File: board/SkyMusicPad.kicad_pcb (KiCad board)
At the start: 2 copper layers, 119.4 x 61 mm, 32 parts, among them SW1 RotaryEncoder_Switch

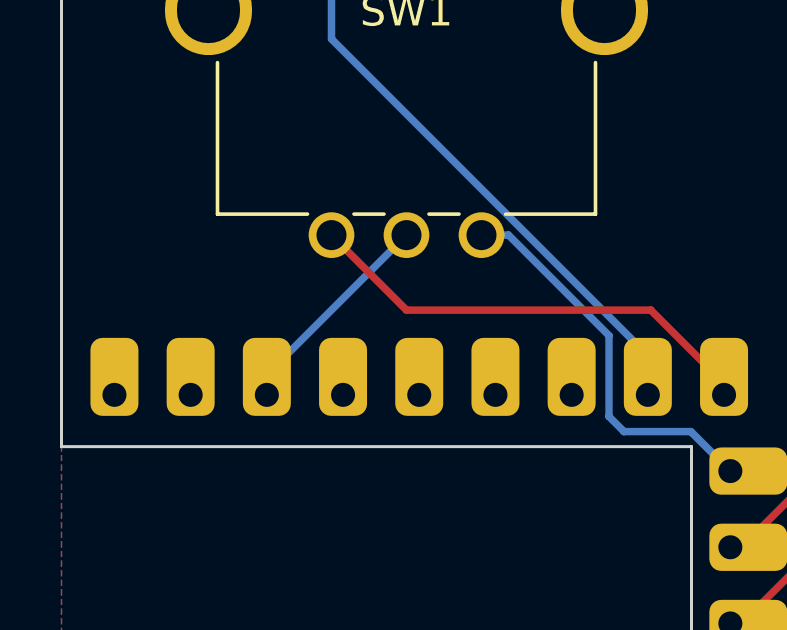
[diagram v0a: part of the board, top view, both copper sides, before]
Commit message: Adjusted rotary encoder to have common point GND
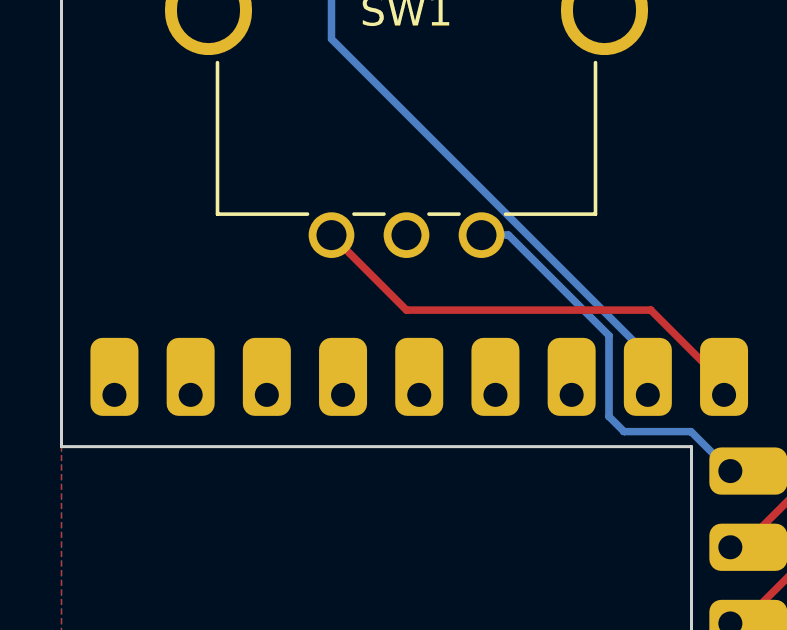
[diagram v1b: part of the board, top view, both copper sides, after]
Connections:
- SW1 pad C: +3.3V -> GND
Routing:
- net +3.3V: track 7.25 -> 0.00 mm
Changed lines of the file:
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@@
       (net 13 "Net-(RZ1-GP13)") (pinfunction "B") (pintype "passive"))
     (pad "C" thru_hole circle (at 0 2.5) (size 1.524 1.524) (drill 1) (layers "*.Cu" "*.Mask")
-      (net 9 "+3.3V") (pinfunction "C") (pintype "passive"))
+      (net 11 "GND") (pinfunction "C") (pintype "passive"))
     (pad "S1" thru_hole circle (at 14.5 0) (size 1.524 1.524) (drill 1) (layers "*.Cu" "*.Mask")
       (net 14 "Net-(RZ1-GP15)") (pinfunction "S1") (pintype "passive"))
@@
   (via (at 109 69.5) (size 0.8) (drill 0.4) (layers "F.Cu" "B.Cu") (net 8))
   (via (at 72.5 69.5) (size 0.8) (drill 0.4) (layers "F.Cu" "B.Cu") (net 8))
-  (segment (start 31.5 47.95) (end 26.845 52.605) (width 0.25) (layer "B.Cu") (net 9))
-  (segment (start 26.845 52.605) (end 26.845 53.275) (width 0.25) (layer "B.Cu") (net 9))
   (segment (start 29 47.95) (end 31.5 50.45) (width 0.25) (layer "F.Cu") (net 12))
   (segment (start 39.645376 50.45) (end 42.085 52.889624) (width 0.25) (layer "F.Cu") (net 12))

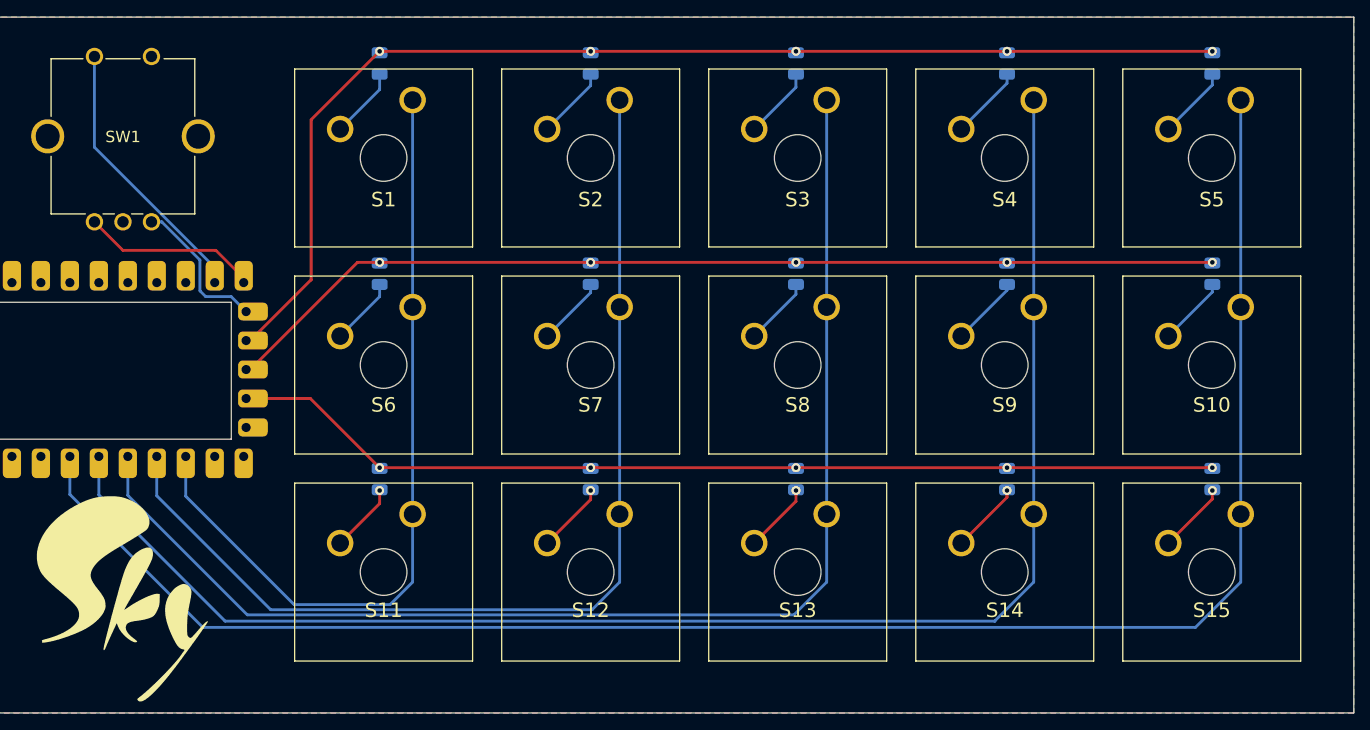
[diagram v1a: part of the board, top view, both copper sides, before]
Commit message: Fixed the use of the incorrect footprint for MX
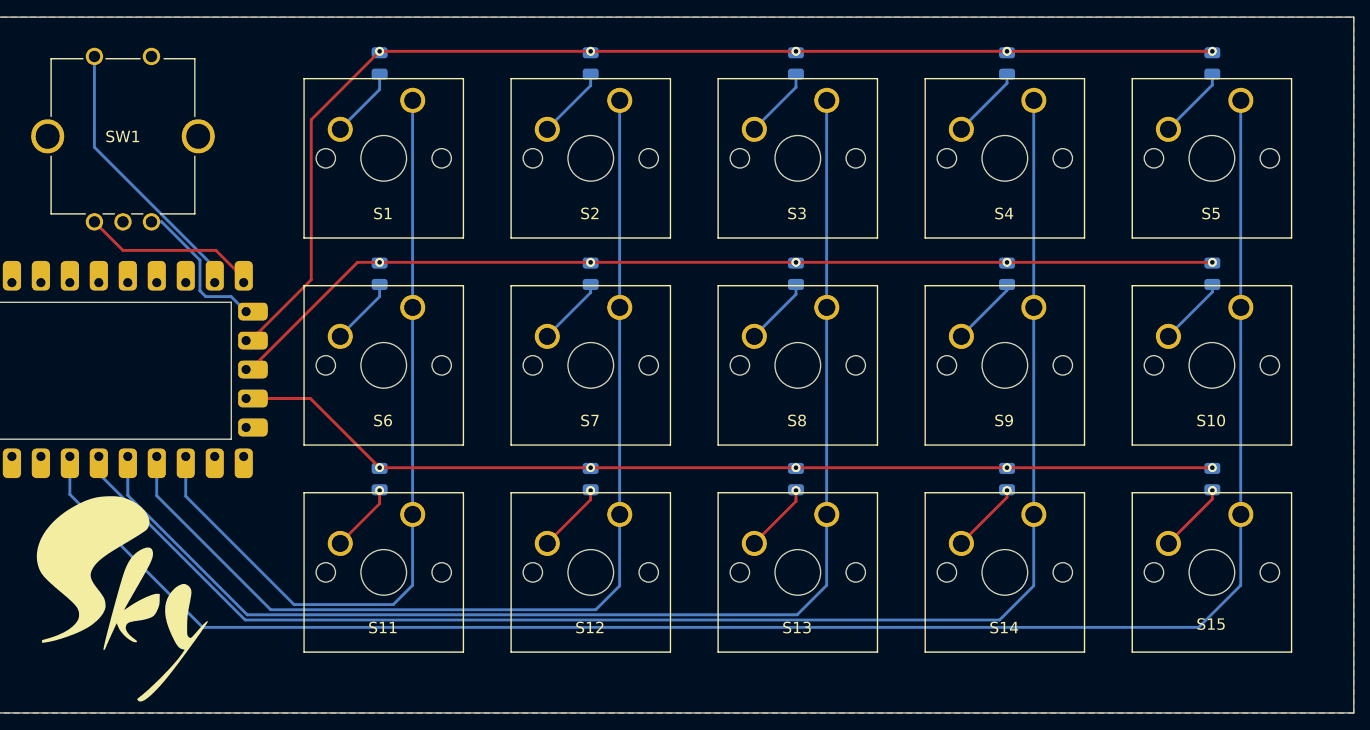
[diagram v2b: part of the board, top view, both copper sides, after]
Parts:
- S1, S10, S11, S12, S13, S14, S15, S2, S3, S4, S5, S6, S7, S8, S9: footprint MX1A-C1NN:MX1AC1NN -> Button_Switch_Keyboard:SW_Cherry_MX_1.00u_PCB
- moved S1 6.84 mm to (56.9, 37.3)
- moved S11 6.84 mm to (56.9, 73.6)
- moved S12 6.84 mm to (75.0, 73.6)
- moved S13 6.84 mm to (93.2, 73.6)
- moved S14 6.84 mm to (111.3, 73.6)
- moved S15 6.84 mm to (129.5, 73.6)
- moved S2 6.84 mm to (75.0, 37.3)
- moved S3 6.84 mm to (93.2, 37.3)
- moved S4 6.84 mm to (111.3, 37.3)
- moved S5 6.84 mm to (129.5, 37.3)
- moved S10 6.84 mm to (129.5, 55.5)
- moved S6 6.84 mm to (56.9, 55.5)
- moved S7 6.84 mm to (75.0, 55.5)
- moved S8 6.84 mm to (93.2, 55.5)
- moved S9 6.84 mm to (111.3, 55.5)
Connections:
- S1 pad 1: Net-(D1-A) -> Col0
- S1 pad 2: Col0 -> Net-(D1-A)
- S11 pad 1: Net-(D3-A) -> Col0
- S11 pad 2: Col0 -> Net-(D3-A)
- S12 pad 1: Net-(D6-A) -> Col1
- S12 pad 2: Col1 -> Net-(D6-A)
- S13 pad 1: Net-(D9-A) -> Col2
- S13 pad 2: Col2 -> Net-(D9-A)
- S14 pad 1: Net-(D12-A) -> Col3
- S14 pad 2: Col3 -> Net-(D12-A)
- S2 pad 1: Net-(D4-A) -> Col1
- S2 pad 2: Col1 -> Net-(D4-A)
- S3 pad 1: Net-(D7-A) -> Col2
- S3 pad 2: Col2 -> Net-(D7-A)
- S4 pad 1: Net-(D10-A) -> Col3
- S4 pad 2: Col3 -> Net-(D10-A)
- S6 pad 1: Net-(D2-A) -> Col0
- S6 pad 2: Col0 -> Net-(D2-A)
- S7 pad 1: Net-(D5-A) -> Col1
- S7 pad 2: Col1 -> Net-(D5-A)
- S8 pad 1: Net-(D8-A) -> Col2
- S8 pad 2: Col2 -> Net-(D8-A)
- S9 pad 1: Net-(D11-A) -> Col3
- S9 pad 2: Col3 -> Net-(D11-A)
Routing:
- net Col3: track 133.6 -> 132.6 mm

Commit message: a
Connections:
- S10 pad 1: Net-(D14-A) -> Col4
- S10 pad 2: Col4 -> Net-(D14-A)
- S15 pad 1: Net-(D15-A) -> Col4
- S15 pad 2: Col4 -> Net-(D15-A)
- S5 pad 1: Net-(D13-A) -> Col4
- S5 pad 2: Col4 -> Net-(D13-A)
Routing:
- net Col3: track 132.6 -> 134.1 mm
- net Net-(D9-A): track 6.13 -> 6.21 mm, vias 1 -> 0
- net Net-(D3-A): track 6.04 -> 6.13 mm, vias 1 -> 0
- net Net-(D6-A): track 6.19 -> 6.28 mm, vias 1 -> 0
- net Net-(D15-A): track 6.21 -> 6.30 mm, vias 1 -> 0
- net Net-(D12-A): track 6.27 -> 6.36 mm, vias 1 -> 0
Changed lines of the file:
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@@
     (pad "" np_thru_hole circle (at 2.54 5.08) (size 1.7 1.7) (drill 1.7) (layers "*.Cu" "*.Mask"))
     (pad "1" thru_hole circle (at 0 0) (size 2.2 2.2) (drill 1.5) (layers "*.Cu" "*.Mask")
-      (net 29 "Net-(D15-A)") (pinfunction "1") (pintype "passive"))
+      (net 5 "Col4") (pinfunction "1") (pintype "passive"))
     (pad "2" thru_hole circle (at -6.35 2.54) (size 2.2 2.2) (drill 1.5) (layers "*.Cu" "*.Mask")
-      (net 5 "Col4") (pinfunction "2") (pintype "passive"))
+      (net 29 "Net-(D15-A)") (pinfunction "2") (pintype "passive"))
     (model "${KICAD6_3DMODEL_DIR}/Button_Switch_Keyboard.3dshapes/SW_Cherry_MX_1.00u_PCB.wrl"
       (offset (xyz 0 0 0))
@@
     (pad "" np_thru_hole circle (at 2.54 5.08) (size 1.7 1.7) (drill 1.7) (layers "*.Cu" "*.Mask"))
     (pad "1" thru_hole circle (at 0 0) (size 2.2 2.2) (drill 1.5) (layers "*.Cu" "*.Mask")
-      (net 27 "Net-(D13-A)") (pinfunction "1") (pintype "passive"))
+      (net 5 "Col4") (pinfunction "1") (pintype "passive"))
     (pad "2" thru_hole circle (at -6.35 2.54) (size 2.2 2.2) (drill 1.5) (layers "*.Cu" "*.Mask")
-      (net 5 "Col4") (pinfunction "2") (pintype "passive"))
+      (net 27 "Net-(D13-A)") (pinfunction "2") (pintype "passive"))
     (model "${KICAD6_3DMODEL_DIR}/Button_Switch_Keyboard.3dshapes/SW_Cherry_MX_1.00u_PCB.wrl"
       (offset (xyz 0 0 0))
@@
     (pad "" np_thru_hole circle (at 2.54 5.08) (size 1.7 1.7) (drill 1.7) (layers "*.Cu" "*.Mask"))
     (pad "1" thru_hole circle (at 0 0) (size 2.2 2.2) (drill 1.5) (layers "*.Cu" "*.Mask")
-      (net 28 "Net-(D14-A)") (pinfunction "1") (pintype "passive"))
+      (net 5 "Col4") (pinfunction "1") (pintype "passive"))
     (pad "2" thru_hole circle (at -6.35 2.54) (size 2.2 2.2) (drill 1.5) (layers "*.Cu" "*.Mask")
-      (net 5 "Col4") (pinfunction "2") (pintype "passive"))
+      (net 28 "Net-(D14-A)") (pinfunction "2") (pintype "passive"))
     (model "${KICAD6_3DMODEL_DIR}/Button_Switch_Keyboard.3dshapes/SW_Cherry_MX_1.00u_PCB.wrl"
       (offset (xyz 0 0 0))
@@
   (gr_line (start 20 67) (end 41 67)
     (stroke (width 0.1) (type default)) (layer "Edge.Cuts"))
-  (segment (start 55.2 81.5) (end 46.5 81.5) (width 0.25) (layer "B.Cu") (net 1))
   (segment (start 56.89 37.27) (end 56.89 79.81) (width 0.25) (layer "B.Cu") (net 1))
-  (segment (start 37.005 72.005) (end 37.005 68.515) (width 0.25) (layer "B.Cu") (net 1))
-  (segment (start 56.89 79.81) (end 55.2 81.5) (width 0.25) (layer "B.Cu") (net 1))
-  (segment (start 46.5 81.5) (end 37.005 72.005) (width 0.25) (layer "B.Cu") (net 1))
-  (segment (start 72.95 81.95) (end 44.45 81.95) (width 0.25) (layer "B.Cu") (net 2))
+  (segment (start 47.005 82) (end 37.005 72) (width 0.25) (layer "B.Cu") (net 1))
+  (segment (start 56.89 79.81) (end 54.7 82) (width 0.25) (layer "B.Cu") (net 1))
+  (segment (start 37.005 72) (end 37.005 68.515) (width 0.25) (layer "B.Cu") (net 1))
+  (segment (start 37.005 72.005) (end 37.005 72) (width 0.25) (layer "B.Cu") (net 1))
+  (segment (start 54.7 82) (end 47.005 82) (width 0.25) (layer "B.Cu") (net 1))
+  (segment (start 44.95 82.45) (end 34.465 71.965) (width 0.25) (layer "B.Cu") (net 2))
   (segment (start 75.04 37.27) (end 75.04 79.86) (width 0.25) (layer "B.Cu") (net 2))
-  (segment (start 44.45 81.95) (end 34.465 71.965) (width 0.25) (layer "B.Cu") (net 2))
+  (segment (start 75.04 79.86) (end 72.45 82.45) (width 0.25) (layer "B.Cu") (net 2))
   (segment (start 34.465 71.965) (end 34.465 68.515) (width 0.25) (layer "B.Cu") (net 2))
-  (segment (start 75.04 79.86) (end 72.95 81.95) (width 0.25) (layer "B.Cu") (net 2))
+  (segment (start 72.45 82.45) (end 44.95 82.45) (width 0.25) (layer "B.Cu") (net 2))
+  (segment (start 93.19 79.81) (end 90.1 82.9) (width 0.25) (layer "B.Cu") (net 3))
+  (segment (start 90.1 82.9) (end 42.9 82.9) (width 0.25) (layer "B.Cu") (net 3))
   (segment (start 31.925 71.925) (end 31.925 68.515) (width 0.25) (layer "B.Cu") (net 3))
-  (segment (start 90.6 82.4) (end 42.4 82.4) (width 0.25) (layer "B.Cu") (net 3))
-  (segment (start 42.4 82.4) (end 31.925 71.925) (width 0.25) (layer "B.Cu") (net 3))
   (segment (start 93.19 37.27) (end 93.19 79.81) (width 0.25) (layer "B.Cu") (net 3))
-  (segment (start 93.19 79.81) (end 90.6 82.4) (width 0.25) (layer "B.Cu") (net 3))
-  (segment (start 42.213604 82.85) (end 108.35 82.85) (width 0.25) (layer "B.Cu") (net 4))
-  (segment (start 29.385 70.021396) (end 42.213604 82.85) (width 0.25) (layer "B.Cu") (net 4))
-  (segment (start 29.385 68.515) (end 29.385 70.021396) (width 0.25) (layer "B.Cu") (net 4))
+  (segment (start 42.9 82.9) (end 31.925 71.925) (width 0.25) (layer "B.Cu") (net 3))
   (segment (start 111.34 79.86) (end 111.34 37.27) (width 0.25) (layer "B.Cu") (net 4))
-  (segment (start 108.35 82.85) (end 111.34 79.86) (width 0.25) (layer "B.Cu") (net 4))
+  (segment (start 111.34 79.86) (end 107.85 83.35) (width 0.25) (layer "B.Cu") (net 4))
+  (segment (start 29.385 68.515) (end 29.385 71.75) (width 0.25) (layer "B.Cu") (net 4))
+  (segment (start 107.85 83.35) (end 40.985 83.35) (width 0.25) (layer "B.Cu") (net 4))
+  (segment (start 40.985 83.35) (end 29.385 71.75) (width 0.25) (layer "B.Cu") (net 4))
+  (segment (start 29.385 71.75) (end 29.385 71.845) (width 0.25) (layer "B.Cu") (net 4))
   (segment (start 26.845 71.845) (end 26.845 68.515) (width 0.25) (layer "B.Cu") (net 5))
   (segment (start 129.49 73.57) (end 129.49 37.27) (width 0.25) (layer "B.Cu") (net 5))
-  (segment (start 129.49 79.81) (end 125.8 83.5) (width 0.25) (layer "B.Cu") (net 5))
+  (segment (start 129.49 79.81) (end 125.5 83.8) (width 0.25) (layer "B.Cu") (net 5))
+  (segment (start 125.5 83.8) (end 38.8 83.8) (width 0.25) (layer "B.Cu") (net 5))
   (segment (start 129.49 73.57) (end 129.49 79.81) (width 0.25) (layer "B.Cu") (net 5))
-  (segment (start 38.5 83.5) (end 26.845 71.845) (width 0.25) (layer "B.Cu") (net 5))
-  (segment (start 125.8 83.5) (end 38.5 83.5) (width 0.25) (layer "B.Cu") (net 5))
+  (segment (start 38.8 83.8) (end 26.845 71.845) (width 0.25) (layer "B.Cu") (net 5))
   (segment (start 129.49 73.57) (end 129.5 73.58) (width 0.25) (layer "B.Cu") (net 5))
   (segment (start 48 39) (end 54 33) (width 0.25) (layer "F.Cu") (net 6))
@@
   (segment (start 54 53.4375) (end 54 54.5) (width 0.25) (layer "B.Cu") (net 16))
   (segment (start 54 54.5) (end 50.54 57.96) (width 0.25) (layer "B.Cu") (net 16))
-  (segment (start 54 71.5) (end 54 72.65) (width 0.25) (layer "F.Cu") (net 17))
-  (segment (start 54 72.65) (end 50.54 76.11) (width 0.25) (layer "F.Cu") (net 17))
-  (via (at 54 71.5) (size 0.8) (drill 0.4) (layers "F.Cu" "B.Cu") (net 17))
+  (segment (start 50.55 76.14) (end 54 72.69) (width 0.25) (layer "B.Cu") (net 17))
+  (segment (start 54 72.69) (end 54 71.4375) (width 0.25) (layer "B.Cu") (net 17))
   (segment (start 72.5 36) (end 68.69 39.81) (width 0.25) (layer "B.Cu") (net 18))
   (segment (start 72.5 35) (end 72.5 36) (width 0.25) (layer "B.Cu") (net 18))
   (segment (start 72.5 54.15) (end 68.69 57.96) (width 0.25) (layer "B.Cu") (net 19))
   (segment (start 72.5 53.4375) (end 72.5 54.15) (width 0.25) (layer "B.Cu") (net 19))
-  (segment (start 72.5 72.3) (end 68.69 76.11) (width 0.25) (layer "F.Cu") (net 20))
-  (segment (start 72.5 71.5) (end 72.5 72.3) (width 0.25) (layer "F.Cu") (net 20))
-  (via (at 72.5 71.5) (size 0.8) (drill 0.4) (layers "F.Cu" "B.Cu") (net 20))
+  (segment (start 68.7 76.14) (end 72.5 72.34) (width 0.25) (layer "B.Cu") (net 20))
+  (segment (start 72.5 72.34) (end 72.5 71.4375) (width 0.25) (layer "B.Cu") (net 20))
   (segment (start 90.5 35) (end 90.5 36.15) (width 0.25) (layer "B.Cu") (net 21))
   (segment (start 90.5 36.15) (end 86.84 39.81) (width 0.25) (layer "B.Cu") (net 21))
   (segment (start 90.5 53.4375) (end 90.5 54.3) (width 0.25) (layer "B.Cu") (net 22))
   (segment (start 90.5 54.3) (end 86.84 57.96) (width 0.25) (layer "B.Cu") (net 22))
-  (segment (start 90.5 72.45) (end 86.84 76.11) (width 0.25) (layer "F.Cu") (net 23))
-  (segment (start 90.5 71.5) (end 90.5 72.45) (width 0.25) (layer "F.Cu") (net 23))
-  (via (at 90.5 71.5) (size 0.8) (drill 0.4) (layers "F.Cu" "B.Cu") (net 23))
+  (segment (start 86.85 76.14) (end 90.5 72.49) (width 0.25) (layer "B.Cu") (net 23))
+  (segment (start 90.5 72.49) (end 90.5 71.4375) (width 0.25) (layer "B.Cu") (net 23))
   (segment (start 109 35) (end 109 35.8) (width 0.25) (layer "B.Cu") (net 24))
   (segment (start 109 35.8) (end 104.99 39.81) (width 0.25) (layer "B.Cu") (net 24))
   (segment (start 109 53.4375) (end 109 53.95) (width 0.25) (layer "B.Cu") (net 25))
   (segment (start 109 53.95) (end 104.99 57.96) (width 0.25) (layer "B.Cu") (net 25))
-  (segment (start 109 71.5) (end 109 72.1) (width 0.25) (layer "F.Cu") (net 26))
-  (segment (start 109 72.1) (end 104.99 76.11) (width 0.25) (layer "F.Cu") (net 26))
-  (via (at 109 71.5) (size 0.8) (drill 0.4) (layers "F.Cu" "B.Cu") (net 26))
+  (segment (start 109 72.14) (end 109 71.4375) (width 0.25) (layer "B.Cu") (net 26))
+  (segment (start 105 76.14) (end 109 72.14) (width 0.25) (layer "B.Cu") (net 26))
   (segment (start 127 35) (end 127 35.95) (width 0.25) (layer "B.Cu") (net 27))
   (segment (start 127 35.95) (end 123.14 39.81) (width 0.25) (layer "B.Cu") (net 27))
   (segment (start 127 53.4375) (end 127 54.1) (width 0.25) (layer "B.Cu") (net 28))
   (segment (start 127 54.1) (end 123.14 57.96) (width 0.25) (layer "B.Cu") (net 28))
-  (segment (start 127 71.5) (end 127 72.25) (width 0.25) (layer "F.Cu") (net 29))
-  (segment (start 127 72.25) (end 123.14 76.11) (width 0.25) (layer "F.Cu") (net 29))
-  (via (at 127 71.5) (size 0.8) (drill 0.4) (layers "F.Cu" "B.Cu") (net 29))
+  (segment (start 123.15 76.14) (end 127 72.29) (width 0.25) (layer "B.Cu") (net 29))
+  (segment (start 127 72.29) (end 127 71.4375) (width 0.25) (layer "B.Cu") (net 29))
   (zone (net 11) (net_name "GND") (layers "F&B.Cu") (hatch edge 0.5)
     (connect_pads (clearance 0.5))
